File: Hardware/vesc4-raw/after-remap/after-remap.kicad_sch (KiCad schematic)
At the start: 26 parts, among them K1 SERVO, P1 HALL/Encoder, P101 CANBUS, P3 PWR_COMM, P4 IN+, P5 IN-, P6 MOTOR1, P7 MOTOR2, P9 MOTOR3, X1 MINI-USB-SHIELD-32005-201

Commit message: export footprint & ngapus warning unmatched
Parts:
- C2: symbol after-remap-rescue:C-RESCUE-BLDC_4 -> vesc4-legacy:C-RESCUE-BLDC_4_4
- C3: symbol after-remap-rescue:C-RESCUE-BLDC_4 -> vesc4-legacy:C-RESCUE-BLDC_4_3
- D1: symbol after-remap-rescue:LED-RESCUE-BLDC_4 -> vesc4-legacy:LED-RESCUE-BLDC_4_5
- D2: symbol after-remap-rescue:LED-RESCUE-BLDC_4 -> vesc4-legacy:LED-RESCUE-BLDC_4_4
- D3: symbol after-remap-rescue:LED-RESCUE-BLDC_4 -> vesc4-legacy:LED-RESCUE-BLDC_4_6
- K1: symbol after-remap-rescue:CONN_3 -> vesc4-legacy:CONN_3_2
- P1: symbol after-remap-rescue:CONN_6 -> vesc4-legacy:CONN_6_2
- P101: symbol after-remap-rescue:CONN_4 -> vesc4-legacy:CONN_4_2
- P3: symbol after-remap-rescue:CONN_01X07 -> vesc4-legacy:CONN_01X07_2
- P4: symbol after-remap-rescue:CONN_1 -> vesc4-legacy:CONN_1_10
- P5: symbol after-remap-rescue:CONN_1 -> vesc4-legacy:CONN_1_9
- P6: symbol after-remap-rescue:CONN_1 -> vesc4-legacy:CONN_1_8
- P7: symbol after-remap-rescue:CONN_1 -> vesc4-legacy:CONN_1_7
- P9: symbol after-remap-rescue:CONN_1 -> vesc4-legacy:CONN_1_6
- R103: symbol after-remap-rescue:R-RESCUE-BLDC_4 -> vesc4-legacy:R-RESCUE-BLDC_4_17
- R104: symbol after-remap-rescue:R-RESCUE-BLDC_4 -> vesc4-legacy:R-RESCUE-BLDC_4_18
- R22: symbol after-remap-rescue:R-RESCUE-BLDC_4 -> vesc4-legacy:R-RESCUE-BLDC_4_15
- R3: symbol after-remap-rescue:R-RESCUE-BLDC_4 -> vesc4-legacy:R-RESCUE-BLDC_4_12
- R37: symbol after-remap-rescue:R-RESCUE-BLDC_4 -> vesc4-legacy:R-RESCUE-BLDC_4_14
- R38: symbol after-remap-rescue:R-RESCUE-BLDC_4 -> vesc4-legacy:R-RESCUE-BLDC_4_13
- R4: symbol after-remap-rescue:R-RESCUE-BLDC_4 -> vesc4-legacy:R-RESCUE-BLDC_4_11
- R5: symbol after-remap-rescue:R-RESCUE-BLDC_4 -> vesc4-legacy:R-RESCUE-BLDC_4_10
- R53: symbol after-remap-rescue:SHUNT -> vesc4-legacy:SHUNT_4
- R54: symbol after-remap-rescue:SHUNT -> vesc4-legacy:SHUNT_3
- R6: symbol after-remap-rescue:R-RESCUE-BLDC_4 -> vesc4-legacy:R-RESCUE-BLDC_4_16
- X1: symbol after-remap-rescue:MINI-USB-SCHIELD-32005-201 -> vesc4-legacy:MINI-USB-SCHIELD-32005-201_2
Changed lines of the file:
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@@
 	(symbol
 		(lib_name "CONN_6_2")
-		(lib_id "after-remap-rescue:CONN_6")
+		(lib_id "vesc4-legacy:CONN_6_2")
 		(at 27.94 118.11 180)
 		(unit 1)
@@
 	(symbol
 		(lib_name "+5V_8")
-		(lib_id "after-remap-rescue:+5V")
+		(lib_id "vesc4-legacy:+5V_8")
 		(at 36.83 124.46 270)
 		(unit 1)
@@
 	(symbol
 		(lib_name "GND-RESCUE-BLDC_4_28")
-		(lib_id "after-remap-rescue:GND-RESCUE-BLDC_4")
+		(lib_id "vesc4-legacy:GND-RESCUE-BLDC_4_28")
 		(at 38.1 111.76 90)
 		(unit 1)
@@
 	(symbol
 		(lib_name "C-RESCUE-BLDC_4_3")
-		(lib_id "after-remap-rescue:C-RESCUE-BLDC_4")
+		(lib_id "vesc4-legacy:C-RESCUE-BLDC_4_3")
 		(at 166.37 146.05 270)
 		(unit 1)
@@
 	(symbol
 		(lib_name "R-RESCUE-BLDC_4_10")
-		(lib_id "after-remap-rescue:R-RESCUE-BLDC_4")
+		(lib_id "vesc4-legacy:R-RESCUE-BLDC_4_10")
 		(at 167.64 140.97 90)
 		(unit 1)
@@
 	(symbol
 		(lib_name "C-RESCUE-BLDC_4_4")
-		(lib_id "after-remap-rescue:C-RESCUE-BLDC_4")
+		(lib_id "vesc4-legacy:C-RESCUE-BLDC_4_4")
 		(at 52.07 60.96 90)
 		(mirror x)
@@
 	(symbol
 		(lib_name "GND-RESCUE-BLDC_4_20")
-		(lib_id "after-remap-rescue:GND-RESCUE-BLDC_4")
+		(lib_id "vesc4-legacy:GND-RESCUE-BLDC_4_20")
 		(at 177.8 148.59 0)
 		(unit 1)
@@
 	(symbol
 		(lib_name "CONN_3_2")
-		(lib_id "after-remap-rescue:CONN_3")
+		(lib_id "vesc4-legacy:CONN_3_2")
 		(at 189.23 143.51 0)
 		(unit 1)
@@
 	(symbol
 		(lib_name "GND-RESCUE-BLDC_4_29")
-		(lib_id "after-remap-rescue:GND-RESCUE-BLDC_4")
+		(lib_id "vesc4-legacy:GND-RESCUE-BLDC_4_29")
 		(at 43.18 63.5 0)
 		(mirror y)
@@
 	(symbol
 		(lib_name "R-RESCUE-BLDC_4_11")
-		(lib_id "after-remap-rescue:R-RESCUE-BLDC_4")
+		(lib_id "vesc4-legacy:R-RESCUE-BLDC_4_11")
 		(at 52.07 57.15 90)
 		(mirror x)
@@
 	(symbol
 		(lib_name "R-RESCUE-BLDC_4_12")
-		(lib_id "after-remap-rescue:R-RESCUE-BLDC_4")
+		(lib_id "vesc4-legacy:R-RESCUE-BLDC_4_12")
 		(at 52.07 54.61 90)
 		(mirror x)
@@
 	(symbol
 		(lib_name "GND-RESCUE-BLDC_4_30")
-		(lib_id "after-remap-rescue:GND-RESCUE-BLDC_4")
+		(lib_id "vesc4-legacy:GND-RESCUE-BLDC_4_30")
 		(at 36.83 138.43 0)
 		(mirror y)
@@
 	(symbol
 		(lib_name "GND-RESCUE-BLDC_4_27")
-		(lib_id "after-remap-rescue:GND-RESCUE-BLDC_4")
+		(lib_id "vesc4-legacy:GND-RESCUE-BLDC_4_27")
 		(at 40.64 87.63 0)
 		(unit 1)
@@
 	(symbol
 		(lib_name "MINI-USB-SCHIELD-32005-201_2")
-		(lib_id "after-remap-rescue:MINI-USB-SCHIELD-32005-201")
+		(lib_id "vesc4-legacy:MINI-USB-SCHIELD-32005-201_2")
 		(at 31.75 80.01 0)
 		(mirror y)
@@
 	(symbol
 		(lib_name "+5V_10")
-		(lib_id "after-remap-rescue:+5V")
+		(lib_id "vesc4-legacy:+5V_10")
 		(at 39.37 133.35 270)
 		(unit 1)
@@
 	(symbol
 		(lib_name "VCC_4")
-		(lib_id "after-remap-rescue:VCC")
+		(lib_id "vesc4-legacy:VCC_4")
 		(at 39.37 135.89 270)
 		(unit 1)
@@
 	(symbol
 		(lib_name "+5V_6")
-		(lib_id "after-remap-rescue:+5V")
+		(lib_id "vesc4-legacy:+5V_6")
 		(at 177.8 137.16 0)
 		(mirror y)
@@
 	(symbol
 		(lib_name "R-RESCUE-BLDC_4_16")
-		(lib_id "after-remap-rescue:R-RESCUE-BLDC_4")
+		(lib_id "vesc4-legacy:R-RESCUE-BLDC_4_16")
 		(at 60.96 74.93 90)
 		(mirror x)
@@
 	(symbol
 		(lib_name "+5V_9")
-		(lib_id "after-remap-rescue:+5V")
+		(lib_id "vesc4-legacy:+5V_9")
 		(at 71.12 73.66 0)
 		(unit 1)
@@
 	(symbol
 		(lib_name "SHUNT_4")
-		(lib_id "after-remap-rescue:SHUNT")
+		(lib_id "vesc4-legacy:SHUNT_4")
 		(at 214.63 123.19 0)
 		(mirror x)
@@
 	(symbol
 		(lib_name "SHUNT_3")
-		(lib_id "after-remap-rescue:SHUNT")
+		(lib_id "vesc4-legacy:SHUNT_3")
 		(at 207.01 110.49 0)
 		(unit 1)
@@
 	(symbol
 		(lib_name "GND-RESCUE-BLDC_4_24")
-		(lib_id "after-remap-rescue:GND-RESCUE-BLDC_4")
+		(lib_id "vesc4-legacy:GND-RESCUE-BLDC_4_24")
 		(at 242.57 128.27 0)
 		(unit 1)
@@
 	(symbol
 		(lib_name "CONN_1_9")
-		(lib_id "after-remap-rescue:CONN_1")
+		(lib_id "vesc4-legacy:CONN_1_9")
 		(at 227.33 35.56 180)
 		(unit 1)
@@
 	(symbol
 		(lib_name "CONN_1_10")
-		(lib_id "after-remap-rescue:CONN_1")
+		(lib_id "vesc4-legacy:CONN_1_10")
 		(at 227.33 30.48 180)
 		(unit 1)
@@
 	(symbol
 		(lib_name "CONN_1_6")
-		(lib_id "after-remap-rescue:CONN_1")
+		(lib_id "vesc4-legacy:CONN_1_6")
 		(at 259.08 68.58 0)
 		(unit 1)
@@
 	(symbol
 		(lib_name "CONN_1_7")
-		(lib_id "after-remap-rescue:CONN_1")
+		(lib_id "vesc4-legacy:CONN_1_7")
 		(at 259.08 72.39 0)
 		(unit 1)
@@
 	(symbol
 		(lib_name "CONN_1_8")
-		(lib_id "after-remap-rescue:CONN_1")
+		(lib_id "vesc4-legacy:CONN_1_8")
 		(at 259.08 92.71 0)
 		(unit 1)
@@
 	(symbol
 		(lib_name "GND-RESCUE-BLDC_4_19")
-		(lib_id "after-remap-rescue:GND-RESCUE-BLDC_4")
+		(lib_id "vesc4-legacy:GND-RESCUE-BLDC_4_19")
 		(at 36.83 102.87 0)
 		(unit 1)
@@
 	(symbol
 		(lib_name "R-RESCUE-BLDC_4_13")
-		(lib_id "after-remap-rescue:R-RESCUE-BLDC_4")
+		(lib_id "vesc4-legacy:R-RESCUE-BLDC_4_13")
 		(at 149.86 162.56 180)
 		(unit 1)
@@
 	(symbol
 		(lib_name "LED-RESCUE-BLDC_4_4")
-		(lib_id "after-remap-rescue:LED-RESCUE-BLDC_4")
+		(lib_id "vesc4-legacy:LED-RESCUE-BLDC_4_4")
 		(at 149.86 173.99 270)
 		(unit 1)
@@
 	(symbol
 		(lib_name "GND-RESCUE-BLDC_4_21")
-		(lib_id "after-remap-rescue:GND-RESCUE-BLDC_4")
+		(lib_id "vesc4-legacy:GND-RESCUE-BLDC_4_21")
 		(at 149.86 179.07 0)
 		(unit 1)
@@
 	(symbol
 		(lib_name "R-RESCUE-BLDC_4_14")
-		(lib_id "after-remap-rescue:R-RESCUE-BLDC_4")
+		(lib_id "vesc4-legacy:R-RESCUE-BLDC_4_14")
 		(at 157.48 162.56 180)
 		(unit 1)
@@
 	(symbol
 		(lib_name "LED-RESCUE-BLDC_4_5")
-		(lib_id "after-remap-rescue:LED-RESCUE-BLDC_4")
+		(lib_id "vesc4-legacy:LED-RESCUE-BLDC_4_5")
 		(at 157.48 173.99 270)
 		(unit 1)
@@
 	(symbol
 		(lib_name "GND-RESCUE-BLDC_4_22")
-		(lib_id "after-remap-rescue:GND-RESCUE-BLDC_4")
+		(lib_id "vesc4-legacy:GND-RESCUE-BLDC_4_22")
 		(at 157.48 179.07 0)
 		(unit 1)
@@
 	(symbol
 		(lib_name "LED-RESCUE-BLDC_4_6")
-		(lib_id "after-remap-rescue:LED-RESCUE-BLDC_4")
+		(lib_id "vesc4-legacy:LED-RESCUE-BLDC_4_6")
 		(at 165.1 173.99 270)
 		(unit 1)
@@
 	(symbol
 		(lib_name "R-RESCUE-BLDC_4_15")
-		(lib_id "after-remap-rescue:R-RESCUE-BLDC_4")
+		(lib_id "vesc4-legacy:R-RESCUE-BLDC_4_15")
 		(at 165.1 162.56 180)
 		(unit 1)
@@
 	(symbol
 		(lib_name "GND-RESCUE-BLDC_4_23")
-		(lib_id "after-remap-rescue:GND-RESCUE-BLDC_4")
+		(lib_id "vesc4-legacy:GND-RESCUE-BLDC_4_23")
 		(at 165.1 179.07 0)
 		(unit 1)
@@
 	(symbol
 		(lib_name "VCC_3")
-		(lib_id "after-remap-rescue:VCC")
+		(lib_id "vesc4-legacy:VCC_3")
 		(at 165.1 156.21 90)
 		(unit 1)
@@
 	(symbol
 		(lib_name "R-RESCUE-BLDC_4_17")
-		(lib_id "after-remap-rescue:R-RESCUE-BLDC_4")
+		(lib_id "vesc4-legacy:R-RESCUE-BLDC_4_17")
 		(at 60.96 77.47 270)
 		(unit 1)
@@
 	(symbol
 		(lib_name "R-RESCUE-BLDC_4_18")
-		(lib_id "after-remap-rescue:R-RESCUE-BLDC_4")
+		(lib_id "vesc4-legacy:R-RESCUE-BLDC_4_18")
 		(at 60.96 80.01 270)
 		(unit 1)
@@
 	(symbol
 		(lib_name "CONN_4_2")
-		(lib_id "after-remap-rescue:CONN_4")
+		(lib_id "vesc4-legacy:CONN_4_2")
 		(at 27.94 99.06 180)
 		(unit 1)
@@
 	(symbol
 		(lib_name "+5V_7")
-		(lib_id "after-remap-rescue:+5V")
+		(lib_id "vesc4-legacy:+5V_7")
 		(at 36.83 95.25 0)
 		(unit 1)
@@
 	(symbol
 		(lib_name "GND-RESCUE-BLDC_4_25")
-		(lib_id "after-remap-rescue:GND-RESCUE-BLDC_4")
+		(lib_id "vesc4-legacy:GND-RESCUE-BLDC_4_25")
 		(at 250.19 128.27 0)
 		(unit 1)
@@
 	(symbol
 		(lib_name "GND-RESCUE-BLDC_4_18")
-		(lib_id "after-remap-rescue:GND-RESCUE-BLDC_4")
+		(lib_id "vesc4-legacy:GND-RESCUE-BLDC_4_18")
 		(at 214.63 129.54 0)
 		(unit 1)
@@
 	(symbol
 		(lib_name "GND-RESCUE-BLDC_4_17")
-		(lib_id "after-remap-rescue:GND-RESCUE-BLDC_4")
+		(lib_id "vesc4-legacy:GND-RESCUE-BLDC_4_17")
 		(at 207.01 116.84 0)
 		(unit 1)
@@
 	(symbol
 		(lib_name "GND-RESCUE-BLDC_4_16")
-		(lib_id "after-remap-rescue:GND-RESCUE-BLDC_4")
+		(lib_id "vesc4-legacy:GND-RESCUE-BLDC_4_16")
 		(at 210.82 104.14 0)
 		(unit 1)
@@
 	(symbol
 		(lib_name "GND-RESCUE-BLDC_4_26")
-		(lib_id "after-remap-rescue:GND-RESCUE-BLDC_4")
+		(lib_id "vesc4-legacy:GND-RESCUE-BLDC_4_26")
 		(at 231.14 38.1 0)
 		(unit 1)
@@
 	(symbol
 		(lib_name "CONN_01X07_2")
-		(lib_id "after-remap-rescue:CONN_01X07")
+		(lib_id "vesc4-legacy:CONN_01X07_2")
 		(at 31.75 140.97 0)
 		(mirror y)

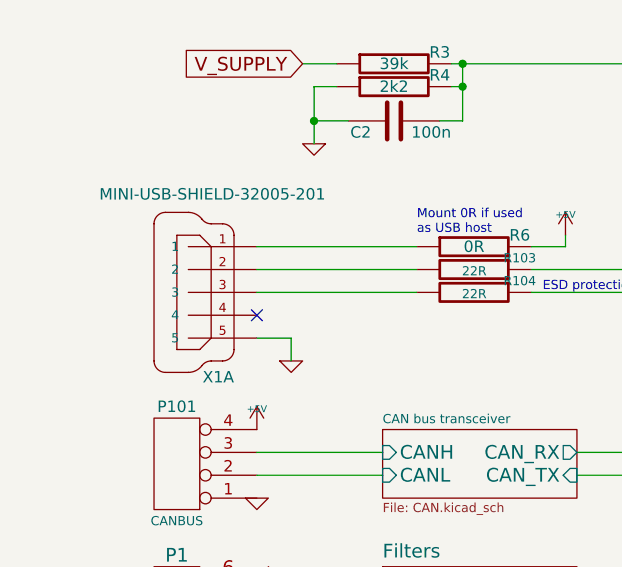
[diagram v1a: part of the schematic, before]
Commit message: ganti kompoinen usb
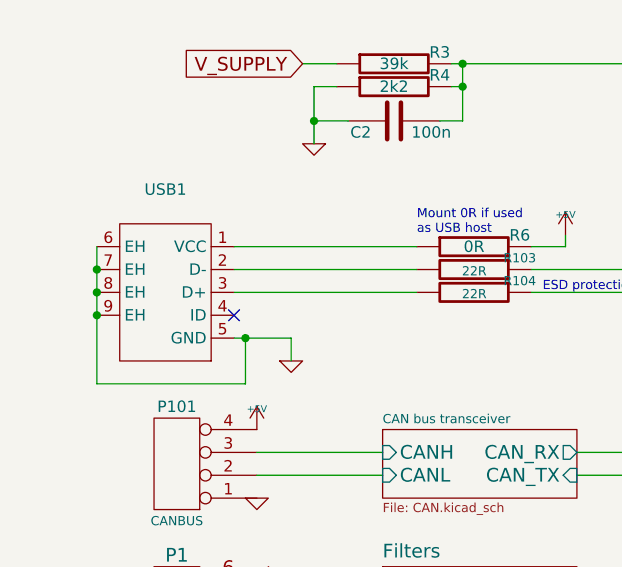
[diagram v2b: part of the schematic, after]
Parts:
- removed X1: MINI-USB-SHIELD-32005-201, CRF1:USB-UX60R-MB-5ST, symbol vesc4-legacy:MINI-USB-SCHIELD-32005-201_2
- added USB1: ~, EasyEDA_Lib:MICRO-USB-SMD_HX-USB-MICRO-XNJ-JB, symbol EasyEDA_Lib:HX USB-MICR XNJ ZB
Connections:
- net GND: now also USB1.5 (GND), USB1.6 (EH), USB1.7 (EH), USB1.8 (EH), USB1.9 (EH)
- net at R6.1: now also USB1.1 (VCC)
- net at R103.2: now also USB1.2 (D-)
- net at R104.2: now also USB1.3 (D+)
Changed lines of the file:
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@@
 	)
 	(junction
+		(at 19.05 80.01)
+		(diameter 0)
+		(color 0 0 0 0)
+	)
+	(junction
 		(at 207.01 101.6)
 		(diameter 0)
@@
 		(color 0 0 0 0)
 	)
+	(junction
+		(at 19.05 77.47)
+		(diameter 0)
+		(color 0 0 0 0)
+	)
+	(junction
+		(at 35.56 85.09)
+		(diameter 0)
+		(color 0 0 0 0)
+	)
+	(junction
+		(at 19.05 82.55)
+		(diameter 0)
+		(color 0 0 0 0)
+	)
 	(no_connect
-		(at 36.83 82.55)
+		(at 34.29 82.55)
 	)
 	(wire
@@
 	(wire
 		(pts
+			(xy 19.05 77.47) (xy 19.05 80.01)
+		)
+		(stroke
+			(width 0)
+			(type default)
+		)
+	)
+	(wire
+		(pts
 			(xy 199.39 113.03) (xy 195.58 113.03)
 		)
@@
 	(wire
 		(pts
-			(xy 36.83 143.51) (xy 82.55 143.51)
+			(xy 34.29 74.93) (xy 54.61 74.93)
 		)
 		(stroke
@@
 	(wire
 		(pts
-			(xy 59.69 54.61) (xy 82.55 54.61)
+			(xy 36.83 143.51) (xy 82.55 143.51)
 		)
 		(stroke
@@
 	(wire
 		(pts
-			(xy 177.8 143.51) (xy 177.8 137.16)
+			(xy 59.69 54.61) (xy 82.55 54.61)
 		)
 		(stroke
@@
 	(wire
 		(pts
-			(xy 210.82 99.06) (xy 219.71 99.06)
+			(xy 177.8 143.51) (xy 177.8 137.16)
 		)
 		(stroke
@@
 	(wire
 		(pts
-			(xy 72.39 158.75) (xy 82.55 158.75)
+			(xy 210.82 99.06) (xy 219.71 99.06)
 		)
 		(stroke
@@
 	(wire
 		(pts
-			(xy 36.83 97.79) (xy 50.8 97.79)
+			(xy 72.39 158.75) (xy 82.55 158.75)
 		)
 		(stroke
@@
 	(wire
 		(pts
-			(xy 39.37 133.35) (xy 36.83 133.35)
+			(xy 36.83 97.79) (xy 50.8 97.79)
 		)
 		(stroke
@@
 	(wire
 		(pts
-			(xy 40.64 85.09) (xy 36.83 85.09)
+			(xy 39.37 133.35) (xy 36.83 133.35)
 		)
 		(stroke
@@
 	(wire
 		(pts
-			(xy 43.18 60.96) (xy 43.18 63.5)
+			(xy 19.05 82.55) (xy 19.05 90.17)
 		)
 		(stroke
@@
 	(wire
 		(pts
-			(xy 59.69 57.15) (xy 59.69 60.96)
+			(xy 43.18 60.96) (xy 43.18 63.5)
 		)
 		(stroke
@@
 	(wire
 		(pts
-			(xy 147.32 113.03) (xy 157.48 113.03)
+			(xy 59.69 57.15) (xy 59.69 60.96)
 		)
 		(stroke
@@
 	(wire
 		(pts
-			(xy 36.83 80.01) (xy 54.61 80.01)
+			(xy 147.32 113.03) (xy 157.48 113.03)
 		)
 		(stroke
@@
 	(wire
 		(pts
+			(xy 34.29 77.47) (xy 54.61 77.47)
+		)
+		(stroke
+			(width 0)
+			(type default)
+		)
+	)
+	(wire
+		(pts
 			(xy 72.39 114.3) (xy 82.55 114.3)
 		)
@@
 	(wire
 		(pts
+			(xy 19.05 80.01) (xy 19.05 82.55)
+		)
+		(stroke
+			(width 0)
+			(type default)
+		)
+	)
+	(wire
+		(pts
 			(xy 147.32 88.9) (xy 157.48 88.9)
 		)
@@
 	(wire
 		(pts
+			(xy 35.56 85.09) (xy 40.64 85.09)
+		)
+		(stroke
+			(width 0)
+			(type default)
+		)
+	)
+	(wire
+		(pts
 			(xy 242.57 125.73) (xy 250.19 125.73)
 		)
@@
 	(wire
 		(pts
+			(xy 34.29 85.09) (xy 35.56 85.09)
+		)
+		(stroke
+			(width 0)
+			(type default)
+		)
+	)
+	(wire
+		(pts
 			(xy 157.48 91.44) (xy 147.32 91.44)
 		)
@@
 	(wire
 		(pts
-			(xy 54.61 74.93) (xy 36.83 74.93)
+			(xy 34.29 80.01) (xy 54.61 80.01)
 		)
 		(stroke
@@
 	(wire
 		(pts
-			(xy 147.32 80.01) (xy 157.48 80.01)
+			(xy 35.56 90.17) (xy 35.56 85.09)
 		)
 		(stroke
@@
 	(wire
 		(pts
-			(xy 157.48 156.21) (xy 157.48 147.32)
+			(xy 147.32 80.01) (xy 157.48 80.01)
 		)
 		(stroke
@@
 	(wire
 		(pts
-			(xy 54.61 77.47) (xy 36.83 77.47)
+			(xy 157.48 156.21) (xy 157.48 147.32)
 		)
 		(stroke
@@
 	(wire
 		(pts
+			(xy 19.05 74.93) (xy 19.05 77.47)
+		)
+		(stroke
+			(width 0)
+			(type default)
+		)
+	)
+	(wire
+		(pts
 			(xy 171.45 146.05) (xy 177.8 146.05)
 		)
@@
 	(wire
 		(pts
+			(xy 19.05 90.17) (xy 35.56 90.17)
+		)
+		(stroke
+			(width 0)
+			(type default)
+		)
+	)
+	(wire
+		(pts
 			(xy 207.01 101.6) (xy 219.71 101.6)
 		)
@@
 	)
 	(symbol
-		(lib_name "MINI-USB-SCHIELD-32005-201_2")
-		(lib_id "vesc4-legacy:MINI-USB-SCHIELD-32005-201_2")
-		(at 31.75 80.01 0)
-		(mirror y)
-		(unit 1)
-		(exclude_from_sim no)
-		(in_bom yes)
-		(on_board yes)
-		(dnp no)
-		(property "Reference" "X1"
-			(at 34.29 90.17 0)
-			(effects
-				(font
-					(size 1.27 1.27)
-				)
-				(justify left bottom)
-			)
-		)
-		(property "Value" "MINI-USB-SHIELD-32005-201"
-			(at 44.45 69.85 0)
-			(effects
-				(font
-					(size 1.27 1.27)
-				)
-				(justify left bottom)
-			)
-		)
-		(property "Footprint" "CRF1:USB-UX60R-MB-5ST"
-			(at 31.75 76.2 0)
-			(effects
-				(font
-					(size 1.27 1.27)
-				)
-				(hide yes)
-			)
-		)
-		(property "Datasheet" ""
-			(at 31.75 80.01 0)
-			(effects
-				(font
-					(size 1.524 1.524)
-				)
-				(hide yes)
-			)
-		)
-		(property "Description" ""
-			(at 31.75 80.01 0)
-			(effects
-				(font
-					(size 1.27 1.27)
-				)
-			)
-		)
-		(pin "5"
-		)
-		(pin "M4"
-		)
-		(pin "M2"
-		)
-		(pin "M1"
-		)
-		(pin "M3"
-		)
-		(pin "1"
-		)
-		(pin "2"
-		)
-		(pin "4"
-		)
-		(pin "3"
-		)
-		(instances
-			(project ""
-				(path "/97cdaedc-7981-4798-95b0-56b9c66aae09"
-					(reference "X1")
-					(unit 1)
-				)
-			)
-		)
-	)
-	(symbol
 		(lib_name "+5V_10")
 		(lib_id "vesc4-legacy:+5V_10")
@@
 					(unit 1)
 				)
+			)
+		)
+	)
+	(symbol
+		(lib_id "EasyEDA_Lib:HX USB-MICR XNJ ZB")
+		(at 26.67 80.01 180)
+		(unit 1)
+		(exclude_from_sim no)
+		(in_bom yes)
+		(on_board yes)
+		(dnp no)
+		(fields_autoplaced yes)
+		(property "Reference" "USB1"
+			(at 26.67 68.58 0)
+			(effects
+				(font
+					(size 1.27 1.27)
+				)
+			)
+		)
+		(property "Value" "~"
+			(at 26.67 71.12 0)
+			(effects
+				(font
+					(size 1.27 1.27)
+				)
+			)
+		)
+		(property "Footprint" "EasyEDA_Lib:MICRO-USB-SMD_HX-USB-MICRO-XNJ-JB"
+			(at 26.67 80.01 0)
+			(effects
+				(font
+					(size 1.27 1.27)
+				)
+				(hide yes)
+			)
+		)
+		(property "Datasheet" ""
+			(at 26.67 80.01 0)
+			(effects
+				(font
+					(size 1.27 1.27)
+				)
+				(hide yes)
+			)
+		)
+		(property "Description" "Connector Type:Micro-B Protocol Standard:USB 2.0 Gender:Female Mounting Type:Surface Mount, Right Angle Number of Contacts:5P Number of Ports:1 Current Rating-Power:1A Voltage Rating:30V Connect-Disconnect Life:3,000 Cycles Supplementary Features:- Center"
+			(at 26.67 80.01 0)
+			(effects
+				(font
+					(size 1.27 1.27)
+				)
+				(hide yes)
+			)
+		)
+		(property "Manufacturer Part" "HX USB-MICR XNJ ZB"
+			(at 26.67 80.01 0)
+			(effects
+				(font
+					(size 1.27 1.27)
+				)
+				(hide yes)
+			)
+		)
+		(property "Manufacturer" "hanxia(韩下)"
+			(at 26.67 80.01 0)
+			(effects
+				(font
+					(size 1.27 1.27)
+				)
+				(hide yes)
+			)
+		)
+		(property "Supplier Part" "C18357557"
+			(at 26.67 80.01 0)
+			(effects
+				(font
+					(size 1.27 1.27)
+				)
+				(hide yes)
+			)
+		)
+		(property "Supplier" "LCSC"
+			(at 26.67 80.01 0)
+			(effects
+				(font
+					(size 1.27 1.27)
+				)
+				(hide yes)
+			)
+		)
+		(property "LCSC Part Name" "Micro-B 母 卧贴"
+			(at 26.67 80.01 0)
+			(effects
+				(font
+					(size 1.27 1.27)
+				)
+				(hide yes)
+			)
+		)
+		(pin "1"
+		)
+		(pin "6"
+		)
+		(pin "5"
+		)
+		(pin "4"
+		)
+		(pin "3"
+		)
+		(pin "2"
+		)
+		(pin "9"
+		)
+		(pin "8"
+		)
+		(pin "7"
+		)
+		(instances
+			(project ""
+				(path "/97cdaedc-7981-4798-95b0-56b9c66aae09"
+					(reference "USB1")
+					(unit 1)
+				)

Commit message: ganti schematic
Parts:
- removed R6: 0R, CRF1:SMD-0603_r, symbol vesc4-legacy:R-RESCUE-BLDC_4_16
- added D6: DIODESCH, Diodes_SMD:SMA_Handsoldering, symbol vesc4-legacy:DIODESCH_2
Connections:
- net +5V: now also D6.2 (K)
- net at USB1.1 (VCC): now also D6.1 (A)
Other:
- note removed: "Mount 0R if used as USB host"
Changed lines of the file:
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@@
 		)
 	)
-	(text "Mount 0R if used\nas USB host"
-		(exclude_from_sim no)
-		(at 54.61 73.66 0)
-		(effects
-			(font
-				(size 1.016 1.016)
-			)
-			(justify left bottom)
-		)
-	)
 	(text "100R if used as\nservo output"
 		(exclude_from_sim no)
@@
 	(wire
 		(pts
+			(xy 64.77 74.93) (xy 71.12 74.93)
+		)
+		(stroke
+			(width 0)
+			(type default)
+		)
+	)
+	(wire
+		(pts
 			(xy 210.82 99.06) (xy 219.71 99.06)
 		)
@@
 	(wire
 		(pts
-			(xy 71.12 74.93) (xy 67.31 74.93)
-		)
-		(stroke
-			(width 0)
-			(type default)
-		)
-	)
-	(wire
-		(pts
 			(xy 147.32 140.97) (xy 160.02 140.97)
 		)
@@
 	)
 	(symbol
-		(lib_name "R-RESCUE-BLDC_4_16")
-		(lib_id "vesc4-legacy:R-RESCUE-BLDC_4_16")
-		(at 60.96 74.93 90)
-		(mirror x)
-		(unit 1)
-		(exclude_from_sim no)
-		(in_bom yes)
-		(on_board yes)
-		(dnp no)
-		(property "Reference" "R6"
-			(at 66.04 73.66 90)
-			(effects
-				(font
-					(size 1.27 1.27)
-				)
-			)
-		)
-		(property "Value" "0R"
-			(at 60.96 74.93 90)
-			(effects
-				(font
-					(size 1.27 1.27)
-				)
-			)
-		)
-		(property "Footprint" "CRF1:SMD-0603_r"
-			(at 60.96 74.93 0)
-			(effects
-				(font
-					(size 1.524 1.524)
-				)
-				(hide yes)
-			)
-		)
-		(property "Datasheet" ""
-			(at 60.96 74.93 0)
-			(effects
-				(font
-					(size 1.524 1.524)
-				)
-				(hide yes)
-			)
-		)
-		(property "Description" ""
-			(at 60.96 74.93 0)
-			(effects
-				(font
-					(size 1.27 1.27)
-				)
-			)
-		)
-		(pin "2"
-		)
-		(pin "1"
-		)
-		(instances
-			(project ""
-				(path "/97cdaedc-7981-4798-95b0-56b9c66aae09"
-					(reference "R6")
-					(unit 1)
-				)
-			)
-		)
-	)
-	(symbol
 		(lib_name "+5V_9")
 		(lib_id "vesc4-legacy:+5V_9")
@@
 		)
 		(property "Value" "+5V"
-			(at 71.12 71.374 0)
+			(at 71.12 70.612 0)
 			(effects
 				(font
@@
 		(on_board yes)
 		(dnp no)
-		(fields_autoplaced yes)
 		(property "Reference" "USB1"
-			(at 26.67 68.58 0)
+			(at 26.67 70.612 0)
 			(effects
 				(font
@@
 					(unit 1)
 				)
+			)
+		)
+	)
+	(symbol
+		(lib_name "DIODESCH_2")
+		(lib_id "vesc4-legacy:DIODESCH_2")
+		(at 59.69 74.93 0)
+		(unit 1)
+		(exclude_from_sim no)
+		(in_bom yes)
+		(on_board yes)
+		(dnp no)
+		(property "Reference" "D6"
+			(at 63.5 73.66 0)
+			(effects
+				(font
+					(size 1.016 1.016)
+				)
+			)
+		)
+		(property "Value" "DIODESCH"
+			(at 59.69 72.136 0)
+			(effects
+				(font
+					(size 1.016 1.016)
+				)
+			)
+		)
+		(property "Footprint" "Diodes_SMD:SMA_Handsoldering"
+			(at 59.69 74.93 0)
+			(effects
+				(font
+					(size 1.524 1.524)
+				)
+				(hide yes)
+			)
+		)
+		(property "Datasheet" ""
+			(at 59.69 74.93 0)
+			(effects
+				(font
+					(size 1.524 1.524)
+				)
+				(hide yes)
+			)
+		)
+		(property "Description" ""
+			(at 59.69 74.93 0)
+			(effects
+				(font
+					(size 1.27 1.27)
+				)
+			)
+		)
+		(pin "1"
+		)
+		(pin "2"
+		)
+		(instances
+			(project "after-remap"
+				(path "/97cdaedc-7981-4798-95b0-56b9c66aae09"
+					(reference "D6")
+					(unit 1)
+				)
